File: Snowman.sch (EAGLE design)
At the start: 11 parts, among them J1 ICSP, U1 ATtiny85

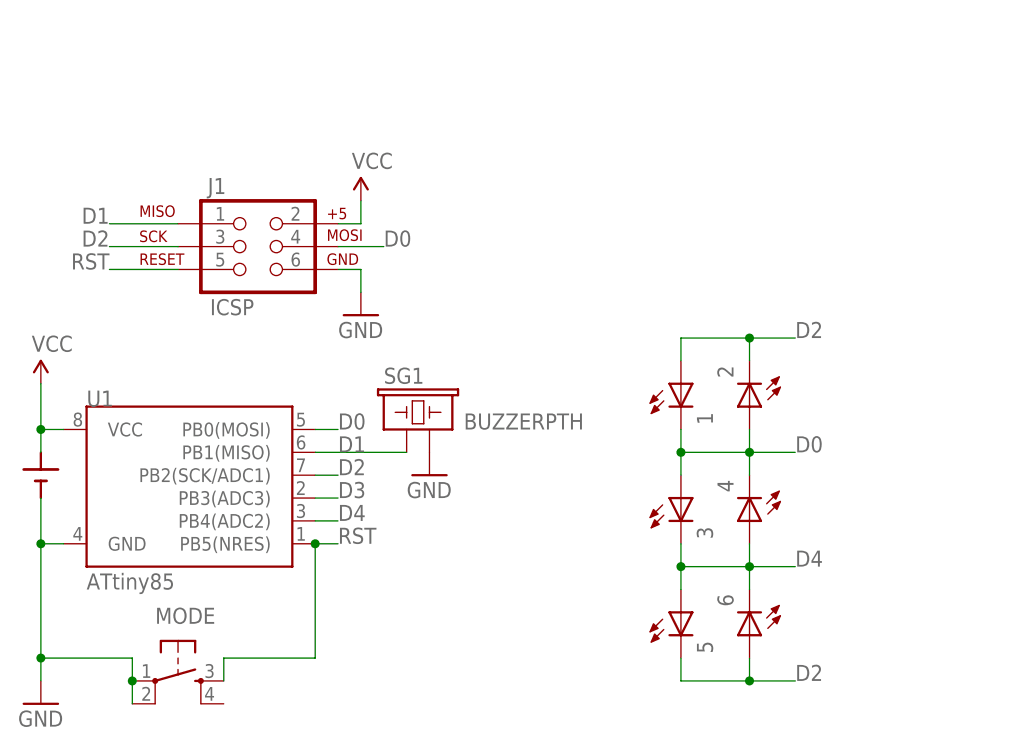
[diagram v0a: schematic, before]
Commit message: updating adding pullup
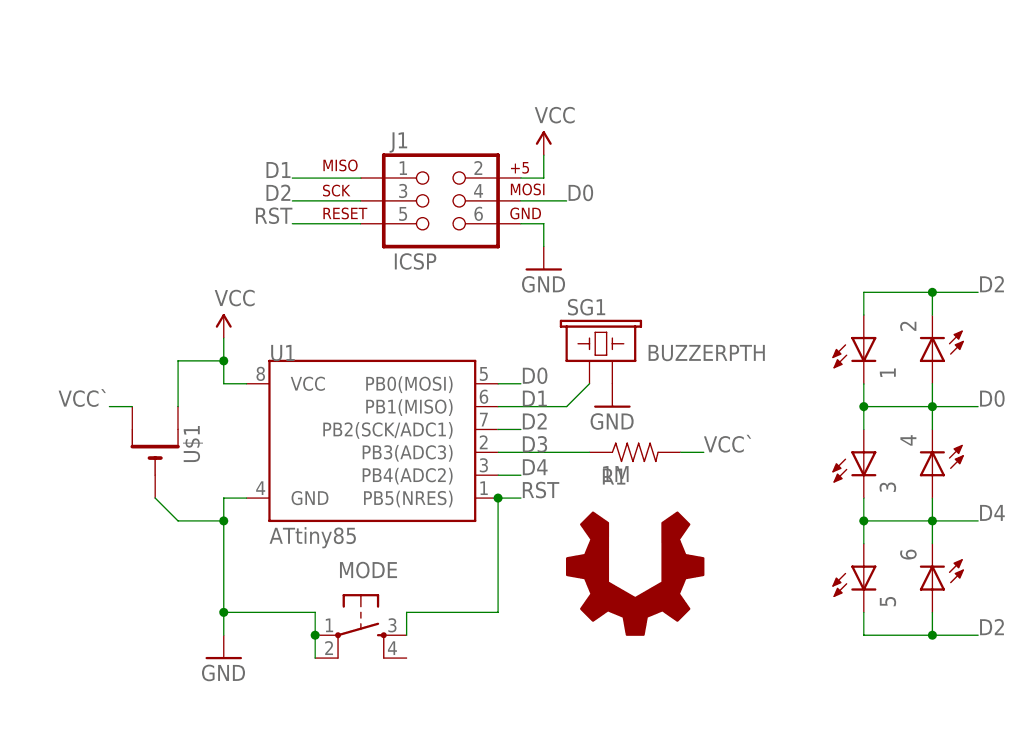
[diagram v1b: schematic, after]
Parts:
- removed BATT: CR2032, battery:BATTCR2032_THRU
- added R1: 1M, barbary_enterprises:RESISTORAXIAL-0.3
- added U$1: (no value), battery:CR2032THM
- added U$2: USER_HACKABLE, logo:USER_HACKABLE
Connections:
- new net VCC`: R1.2, U$1.+1
- net D3: now also R1.1
- net GND: now also U$1.-; no longer BATT.-
- net VCC: now also U$1.+; no longer BATT.+
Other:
- moved on the sheet: 1, 2, 3, 4, 5, 6, J1, MODE, SG1, U1

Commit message: 4H logo
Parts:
- U$2: value USER_HACKABLE -> 18 USC 707; device logo:USER_HACKABLE -> 4h:4H-LOGO6
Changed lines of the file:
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@@
 <part name="R1" library="barbary_enterprises" deviceset="RESISTOR" device="AXIAL-0.3" value="1M"/>
 <part name="U$1" library="battery" deviceset="CR2032" device="THM"/>
-<part name="U$2" library="logo" deviceset="USER_HACKABLE" device=""/>
+<part name="U$2" library="4h" deviceset="4H-LOGO" device="6" value="18 USC 707"/>
 </parts>
 <sheets>
@@
 </instance>
 <instance part="U$1" gate="G$1" x="22.86" y="35.56" rot="MR90"/>
-<instance part="U$2" gate="G$1" x="76.2" y="22.86"/>
+<instance part="U$2" gate="G$1" x="93.98" y="71.12"/>
 </instances>
 <busses>
